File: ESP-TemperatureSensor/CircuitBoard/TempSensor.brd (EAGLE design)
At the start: 33 x 55.9 mm, 9 parts

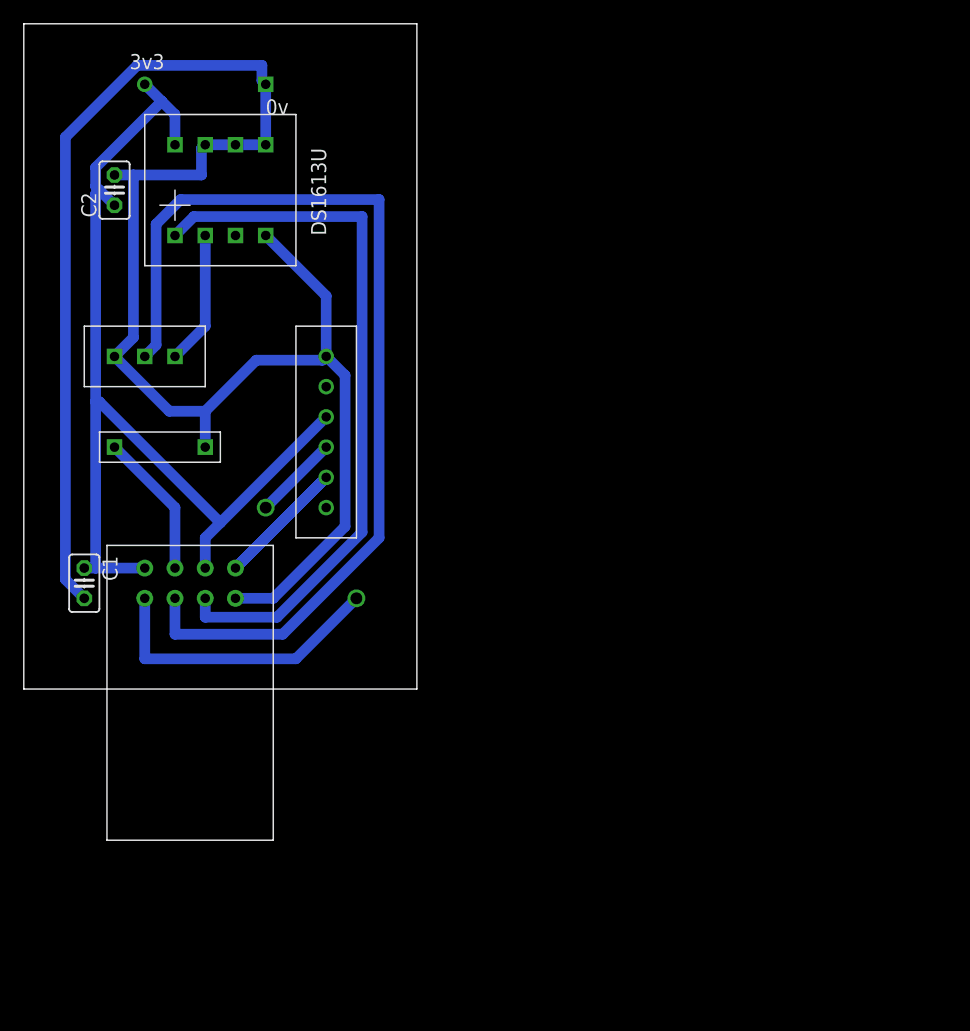
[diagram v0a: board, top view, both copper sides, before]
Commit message: Uploaded circuit diagram and improved PCB design
PCB design for simple prototyping fabing. Single sided with large
tracks.
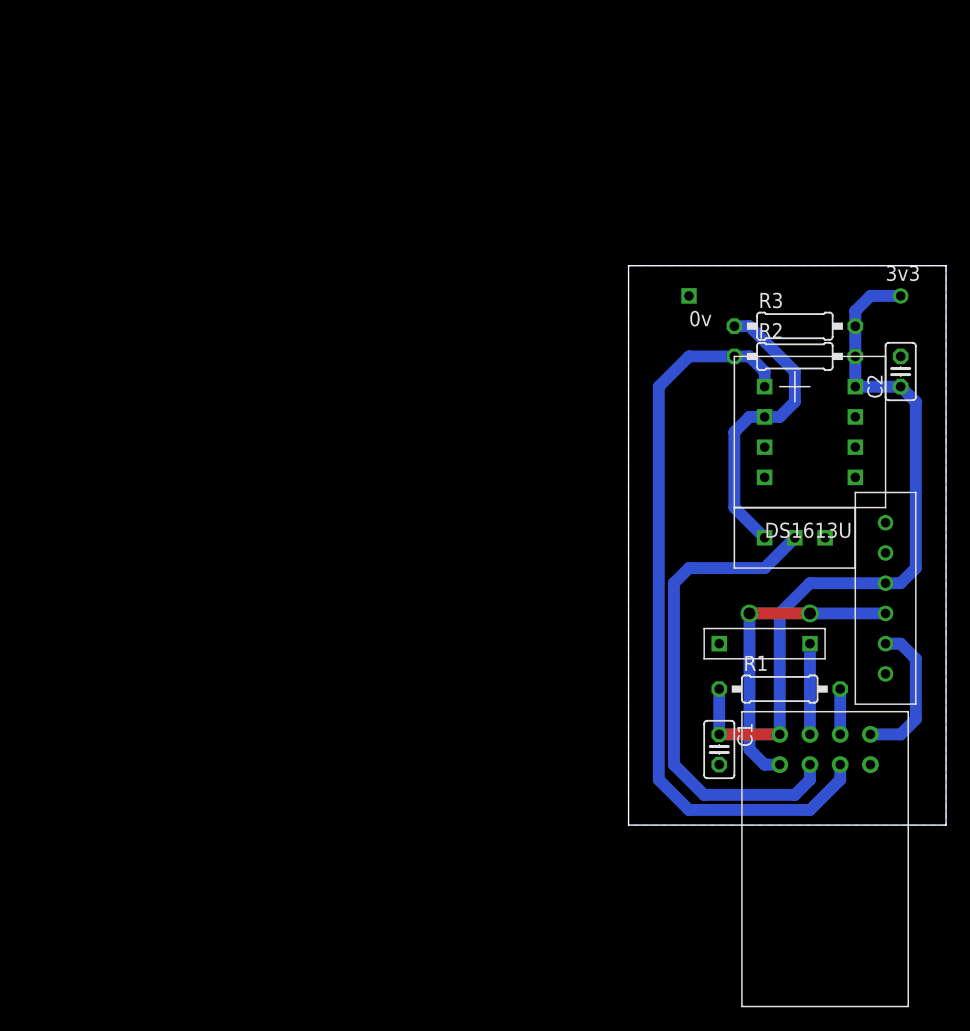
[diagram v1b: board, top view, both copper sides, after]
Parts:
- added R1, R2, R3: (no value), rcl:0207/10
- moved C2 67.8 mm to (68.6, 54.6)
- moved U$6 65.9 mm to (68.6, 61.0)
- moved U$4 56.7 mm to (59.7, 40.6), turned to 0 degrees
- moved U$3 55.9 mm to (62.2, 50.8), turned to 0 degrees
- moved U$2 55.8 mm to (58.4, 31.8), turned to 0 degrees
- moved C1 55.1 mm to (53.3, 22.9)
- moved U$1 55.1 mm to (66.0, 24.1)
- moved U$5 49.0 mm to (67.3, 39.4)
- moved U$7 39.8 mm to (50.8, 61.0)
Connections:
- new net N$8: R1.2, U$1.P$2
- net +3V3: now also R1.1, R2.2, R3.2; no longer U$1.P$2
- net N$3: now also R3.1
- net N$4: now also R2.1
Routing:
- net GND: track 159.7 -> 0.00 mm
- net N$1: track 83.0 -> 41.3 mm
- net +3V3: track 86.4 -> 62.3 mm
- net N$3: track 11.2 -> 25.3 mm
- net N$6: track 21.6 -> 12.5 mm
- net N$5: track 32.1 -> 25.9 mm
- net N$2: track 12.3 -> 7.62 mm
- net N$8: track 0.00 -> 3.81 mm
- net N$4: track 60.6 -> 63.4 mm
- added copper zone on layer 16, net GND
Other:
- board size 33 x 55.9 mm -> 26.7 x 47 mm
